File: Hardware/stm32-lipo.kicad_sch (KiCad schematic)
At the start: 30 parts, among them CN1 B2B-PH-K-S(LF)(SN), U1 STM32G070RBT6, U2 AMS1117, Y1 Crystal_GND24

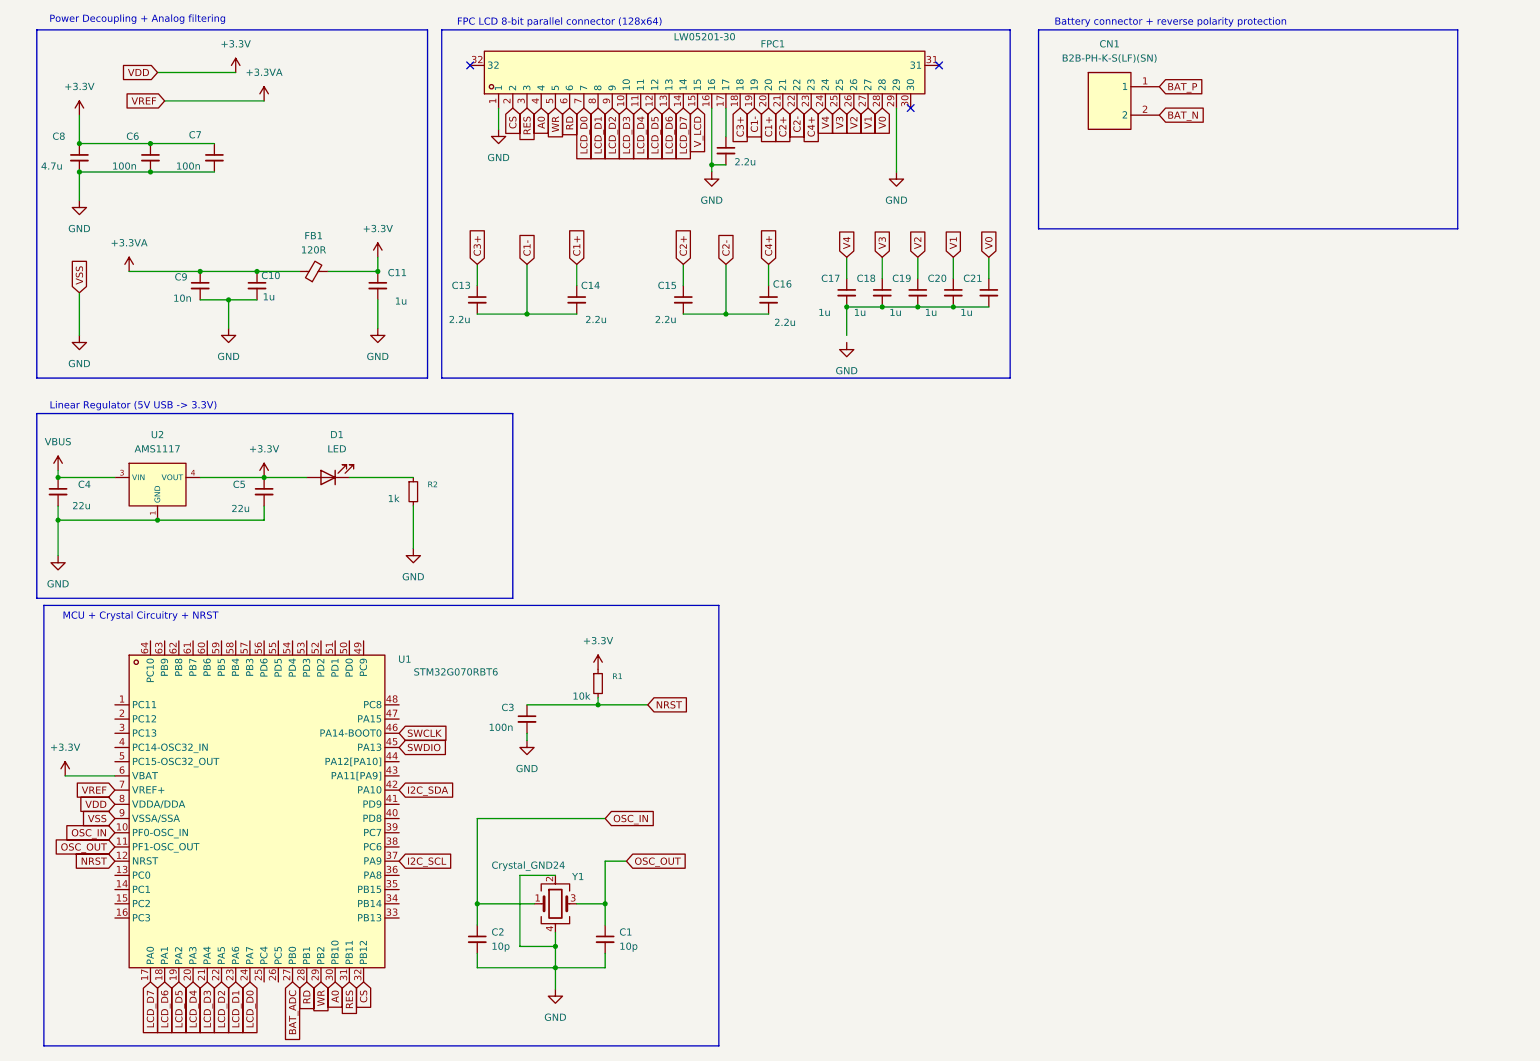
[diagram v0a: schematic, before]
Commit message: Add boilerplate STM32 CubeMX project, add SWD & I2C connector and ADC scaling circuit for battery voltage reading
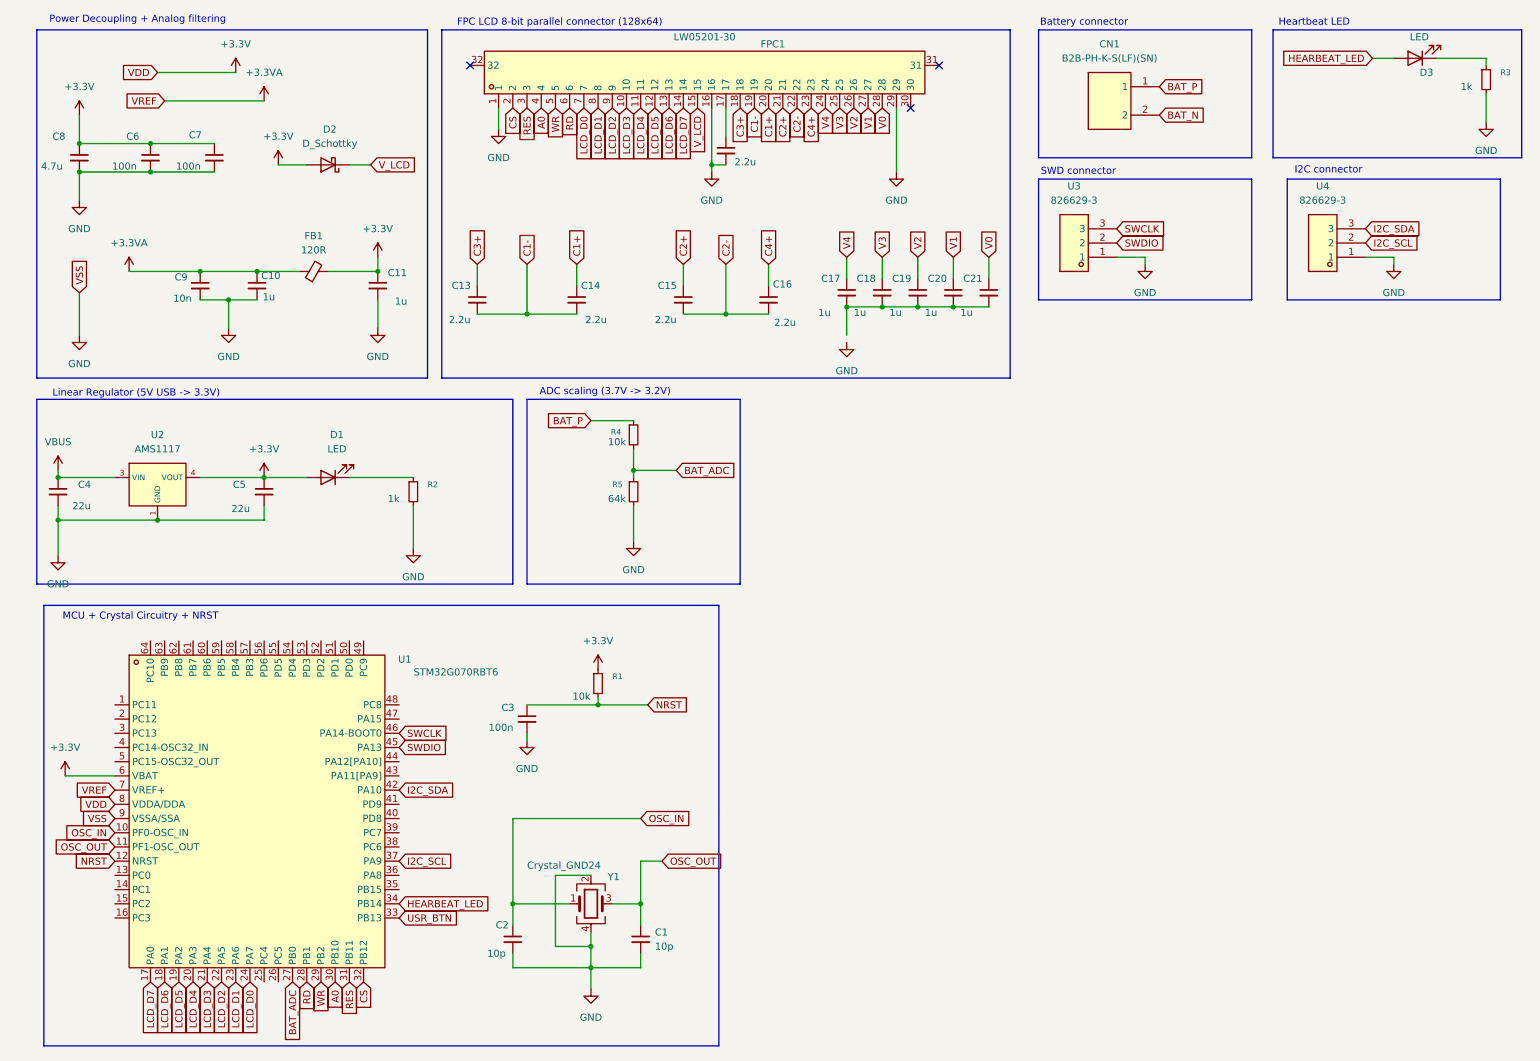
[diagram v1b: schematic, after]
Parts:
- added D2: D_Schottky, symbol Device:D_Schottky
- added D3: LED, symbol Device:LED
- added R3: 1k, symbol Device:R_Small
- added R4: 10k, symbol Device:R_Small
- added R5: 64k, symbol Device:R_Small
- added U3, U4: 826629-3, easyeda2kicad:HDR-TH_3P-P2.54-V-M-1, symbol easyeda2kicad:826629-3
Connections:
- net +3.3V: now also D2.2 (A)
- net BAT_ADC: now also R4.2, R5.1
- net BAT_P: now also R4.1
- net GND: now also R3.2, R5.2, U3.1, U4.1
- net I2C_SCL: now also U4.2
- net I2C_SDA: now also U4.3
- net SWCLK: now also U3.3
- net SWDIO: now also U3.2
- net V_LCD: now also D2.1 (K)
- net USR_BTN: now reaches U1.33 (PB13)
- net HEARBEAT_LED: now reaches U1.34 (PB14)
- net HEARBEAT_LED: now also D3.2 (A)
- new net: D3.1 (K), R3.1
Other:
- note added: "ADC scaling (3.7V -> 3.2V)"
- note added: "Battery connector"
- note added: "Heartbeat LED"
- note added: "I2C connector"
- note added: "SWD connector"
- note removed: "Battery connector + reverse polarity protection"
- moved on the sheet: C1, C2, Y1

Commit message: Progressing on hardware, BQ27441 circuit
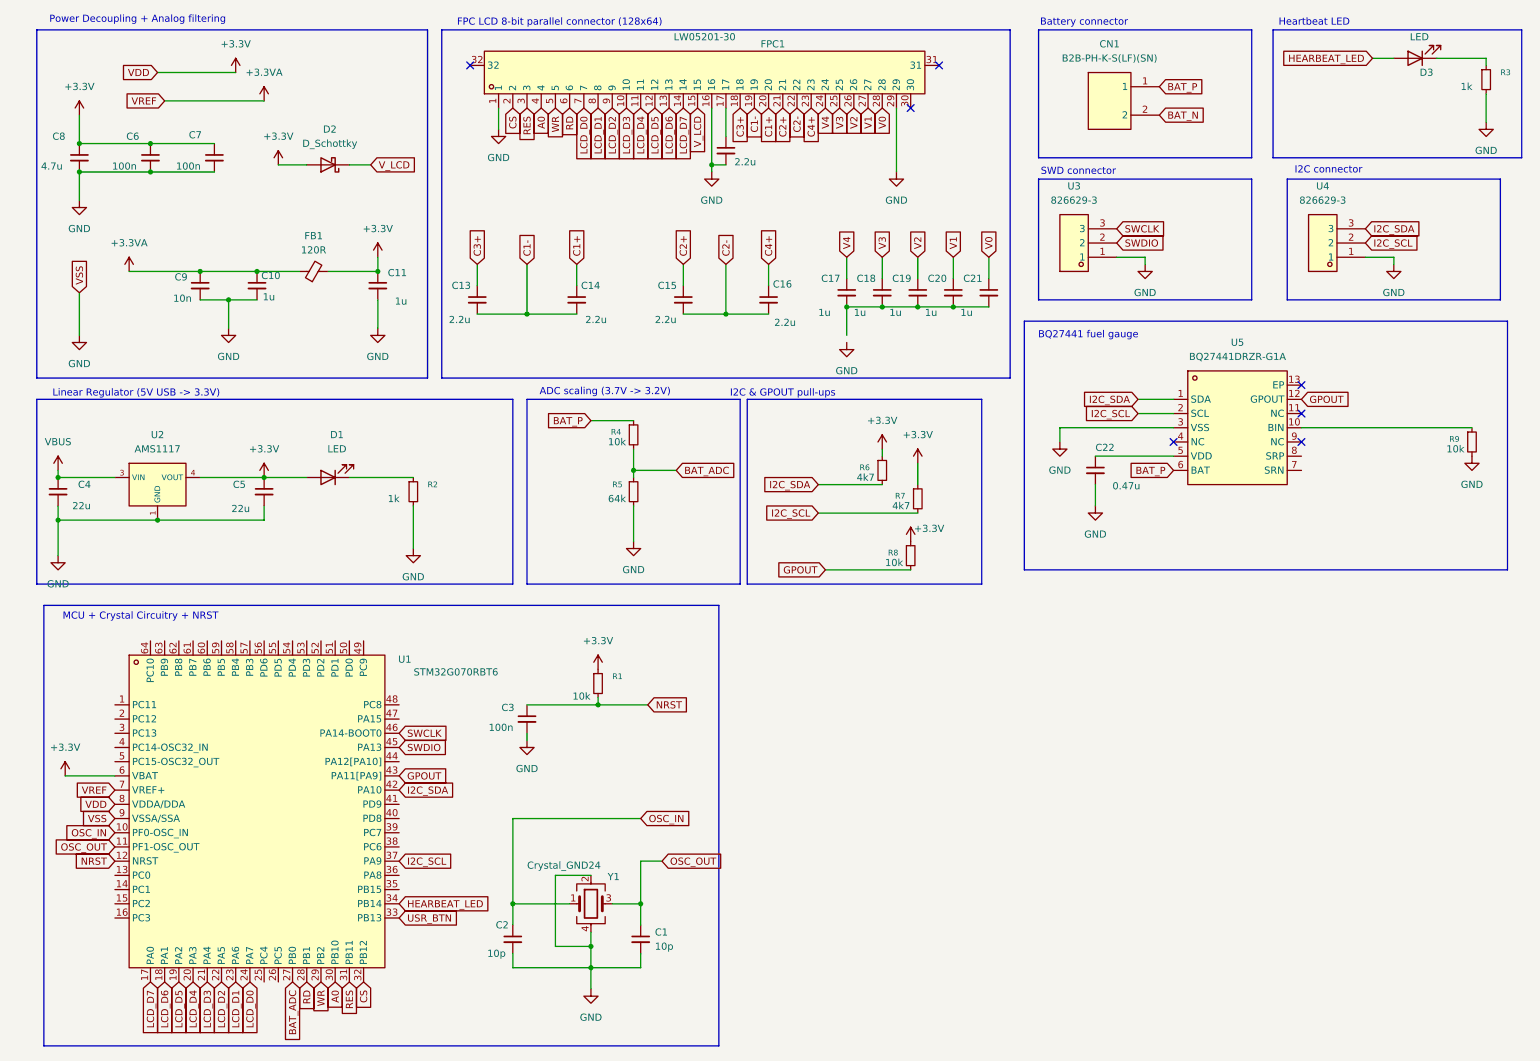
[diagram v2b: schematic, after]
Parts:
- added C22: 0.47u, symbol Device:C_Small
- added R6, R7: 4k7, symbol Device:R_Small
- added R8, R9: 10k, symbol Device:R_Small
- added U5: BQ27441DRZR-G1A, easyeda2kicad:SON-12_L4.0-W2.5-P0.40-BL-EP, symbol easyeda2kicad:BQ27441DRZR-G1A
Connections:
- net +3.3V: now also R6.1, R7.1, R8.1
- net BAT_P: now also U5.6 (BAT)
- net GND: now also C22.2, R9.2, U5.3 (VSS)
- net I2C_SCL: now also R7.2, U5.2 (SCL)
- net I2C_SDA: now also R6.2, U5.1 (SDA)
- net GPOUT: now reaches U1.43 (PA11[PA9])
- net GPOUT: now also R8.2, U5.12 (GPOUT)
- new net: R9.1, U5.10 (BIN)
- new net: C22.1, U5.5 (VDD)
- no-connect marks 3 -> 7
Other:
- note added: "BQ27441 fuel gauge"
- note added: "I2C & GPOUT pull-ups"

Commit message: Update schematics, 3.7V LiPo input to 3.3 voltage rail, BQ27441
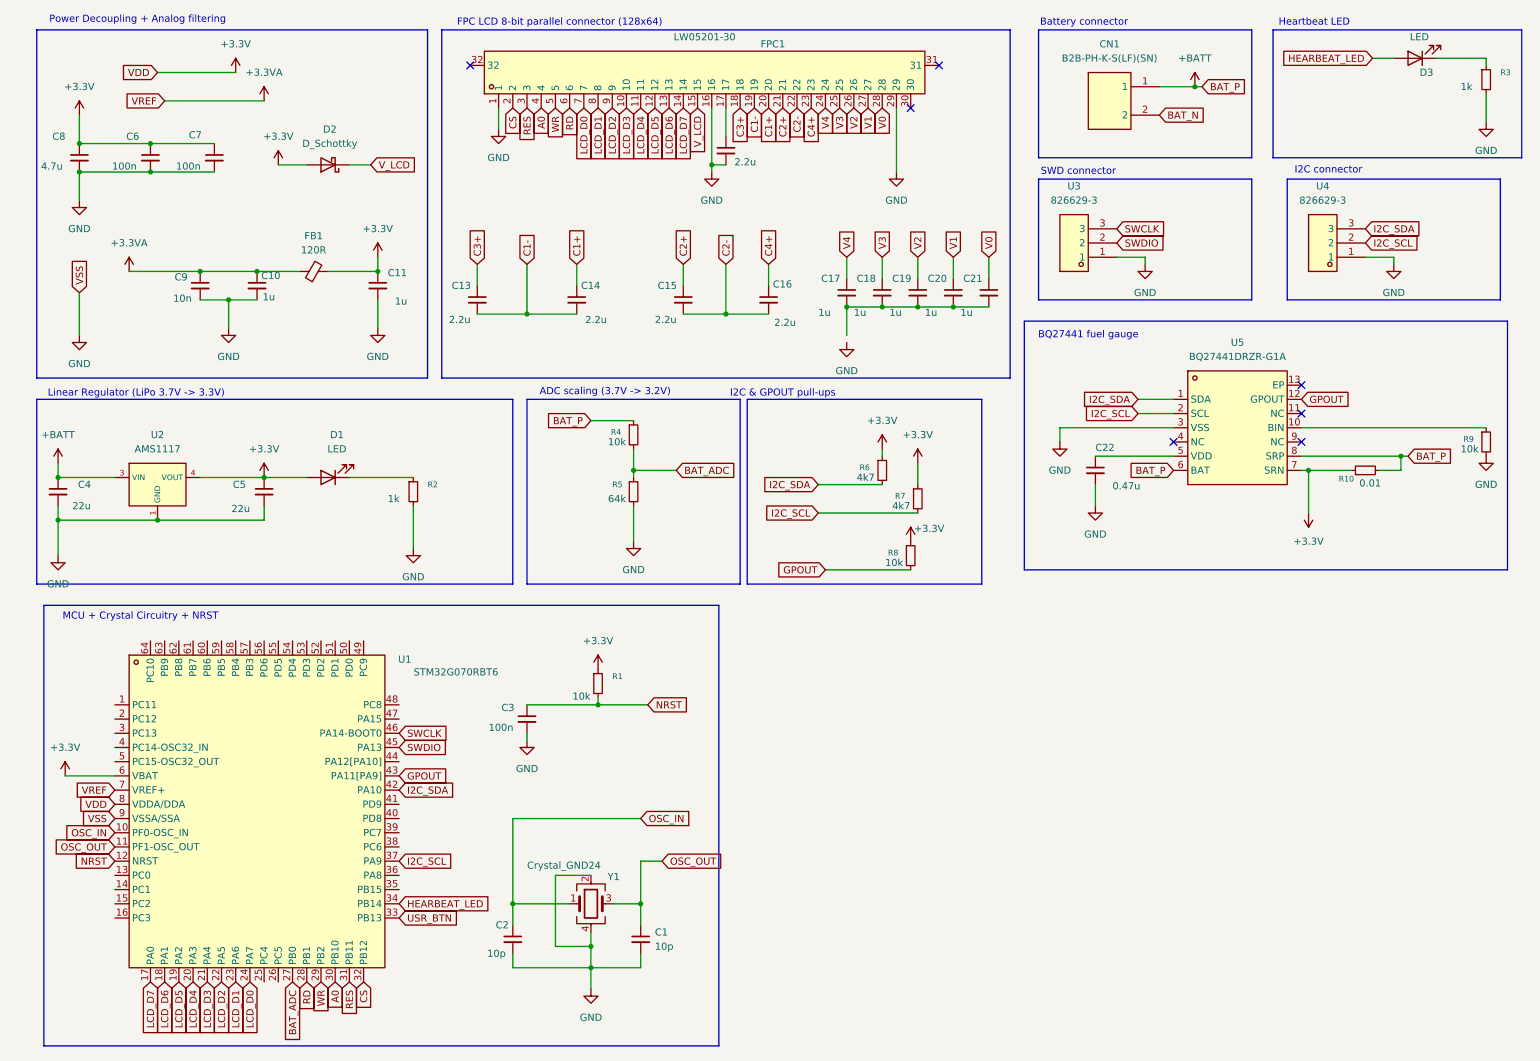
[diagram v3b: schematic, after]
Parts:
- added R10: 0.01, symbol Device:R_Small
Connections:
- net BAT_P is gone; now on net +BATT: CN1.1, R4.1, U5.6 (BAT)
- net VBUS is gone; now on net +BATT: C4.1, U2.3 (VIN)
- net +3.3V: now also U5.7 (SRN), R10.1
- net +BATT: now reaches U5.8 (SRP)
- net +BATT: now also R10.2
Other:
- note added: "Linear Regulator (LiPo 3.7V -> 3.3V)"
- note removed: "Linear Regulator (5V USB -> 3.3V)"
- moved on the sheet: R9

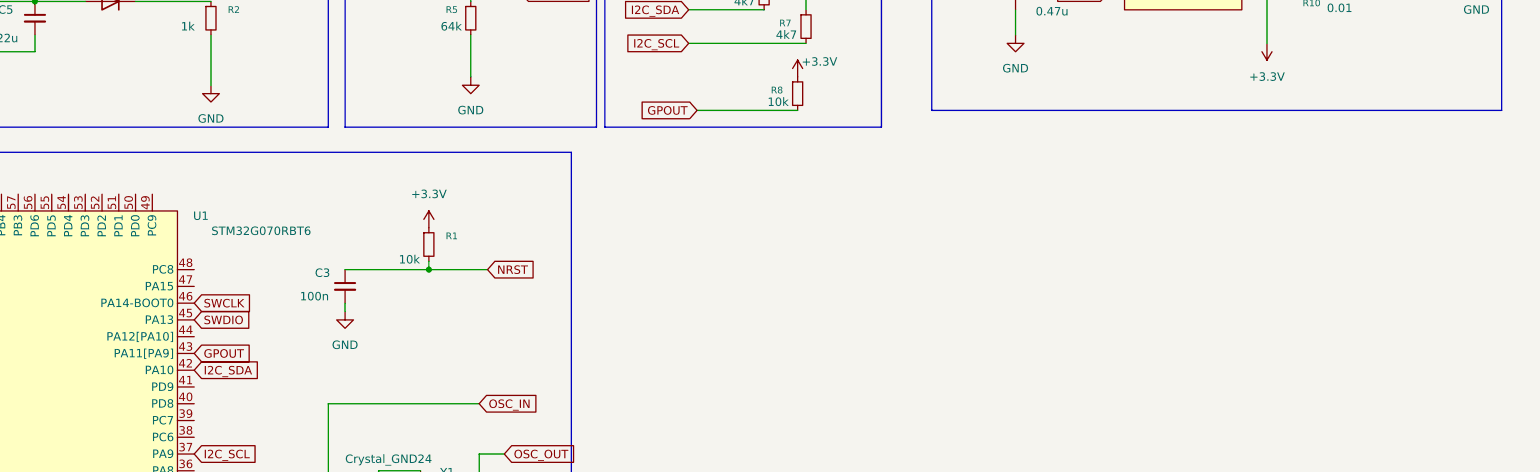
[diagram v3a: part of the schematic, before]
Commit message: Passive buzzer circuitry
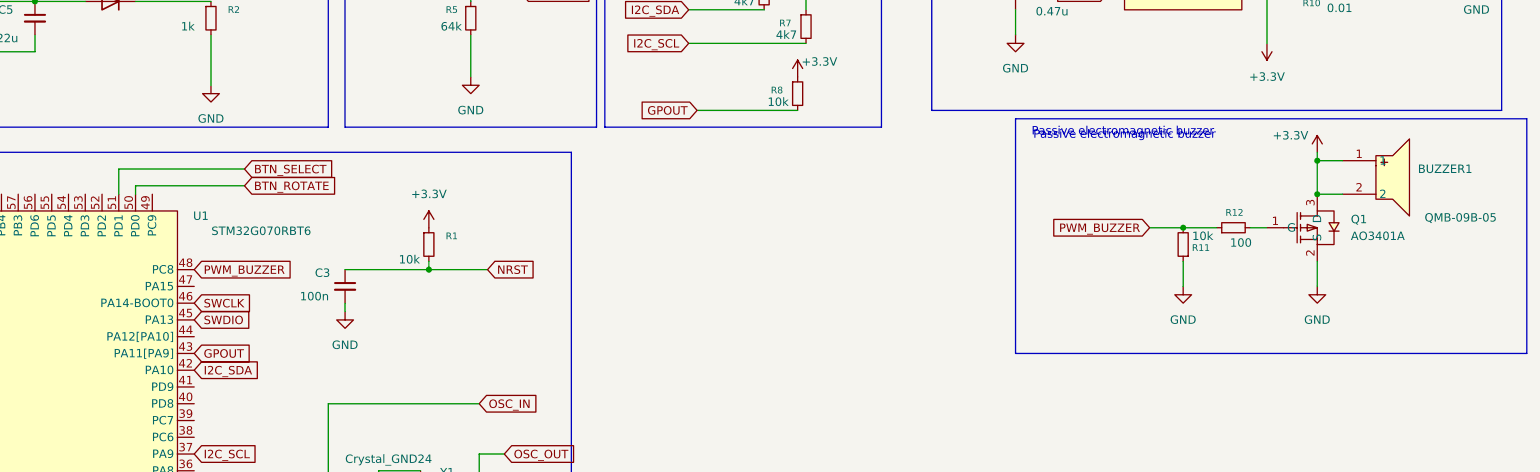
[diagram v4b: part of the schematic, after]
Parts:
- added BUZZER1: QMB-09B-05, easyeda2kicad:BUZ-TH_BD9.0-P4.00-D0.6-FD, symbol easyeda2kicad:QMB-09B-05
- added Q1: AO3401A, easyeda2kicad:SOT-23_L2.9-W1.3-P1.90-LS2.4-BR, symbol easyeda2kicad:AO3401A
- added R11: 10k, symbol Device:R_Small
- added R12: 100, symbol Device:R_Small
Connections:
- net +3.3V: now also BUZZER1.1, BUZZER1.2, Q1.3 (D)
- net GND: now also Q1.2 (S), R11.1
- net PWM_BUZZER: now reaches U1.48 (PC8)
- net PWM_BUZZER: now also R11.2, R12.1
- net BTN_ROTATE: now reaches U1.50 (PD0)
- net BTN_SELECT: now reaches U1.51 (PD1)
- new net: Q1.1 (G), R12.2
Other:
- note added: "Passive electromagnetic buzzer"
